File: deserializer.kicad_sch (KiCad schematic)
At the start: 0 parts

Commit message: [#51601] add deserializer
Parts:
- added C? (x5): C_10u_0402, antmicro-footprints:C_0402_1005Metric, symbol antmicroCapacitors0402:C_10u_0402
- added C? (x7): C_100n_0402, antmicro-footprints:C_0402_1005Metric, symbol antmicroCapacitors0402:C_100n_0402
- added C? (x5): C_10n_0402, antmicro-footprints:C_0402_1005Metric, symbol antmicroCapacitors0402:C_10n_0402
- added R? (x3): R_0R_0402, antmicro-footprints:R_0402_1005Metric, symbol antmicroResistors0402:R_0R_0402
- added R?: R_402R_0402, antmicro-footprints:R_0402_1005Metric, symbol antmicroResistors0402:R_402R_0402
- added U?: MAX96724GTN_VY+, antmicro-footprints:QFN-56-1EP_8x8mm_P0.5mm_EP4.8x4.8mm, symbol antmicroInterfaceControllers:MAX96724GTN_VY+
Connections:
- new net: C?.2, C?.2, C?.2, C?.2, C?.2, R?.1, U?.55 (VDD), U?.56 (VDD)
- new net: C?.2, C?.2, C?.2, C?.2, U?.20 (CAP_VDD), U?.8 (CAP_VDD)
- new net: C?.2, C?.2, C?.2, C?.2, C?.2, R?.1, U?.21 (VDD_1.8V), U?.7 (VDD_1.8V)
- new net: C?.2, C?.2, C?.2, R?.1, U?.24 (VDDIO)
- new net +1V8: R?.2
- new net GND: C?.1, C?.1, C?.1, C?.1, C?.1, C?.1, C?.1, C?.1, C?.1, C?.1, C?.1, C?.1, C?.1, C?.1, C?.1, C?.1, C?.1, U?.57 (GND)
- new net VDD: R?.2

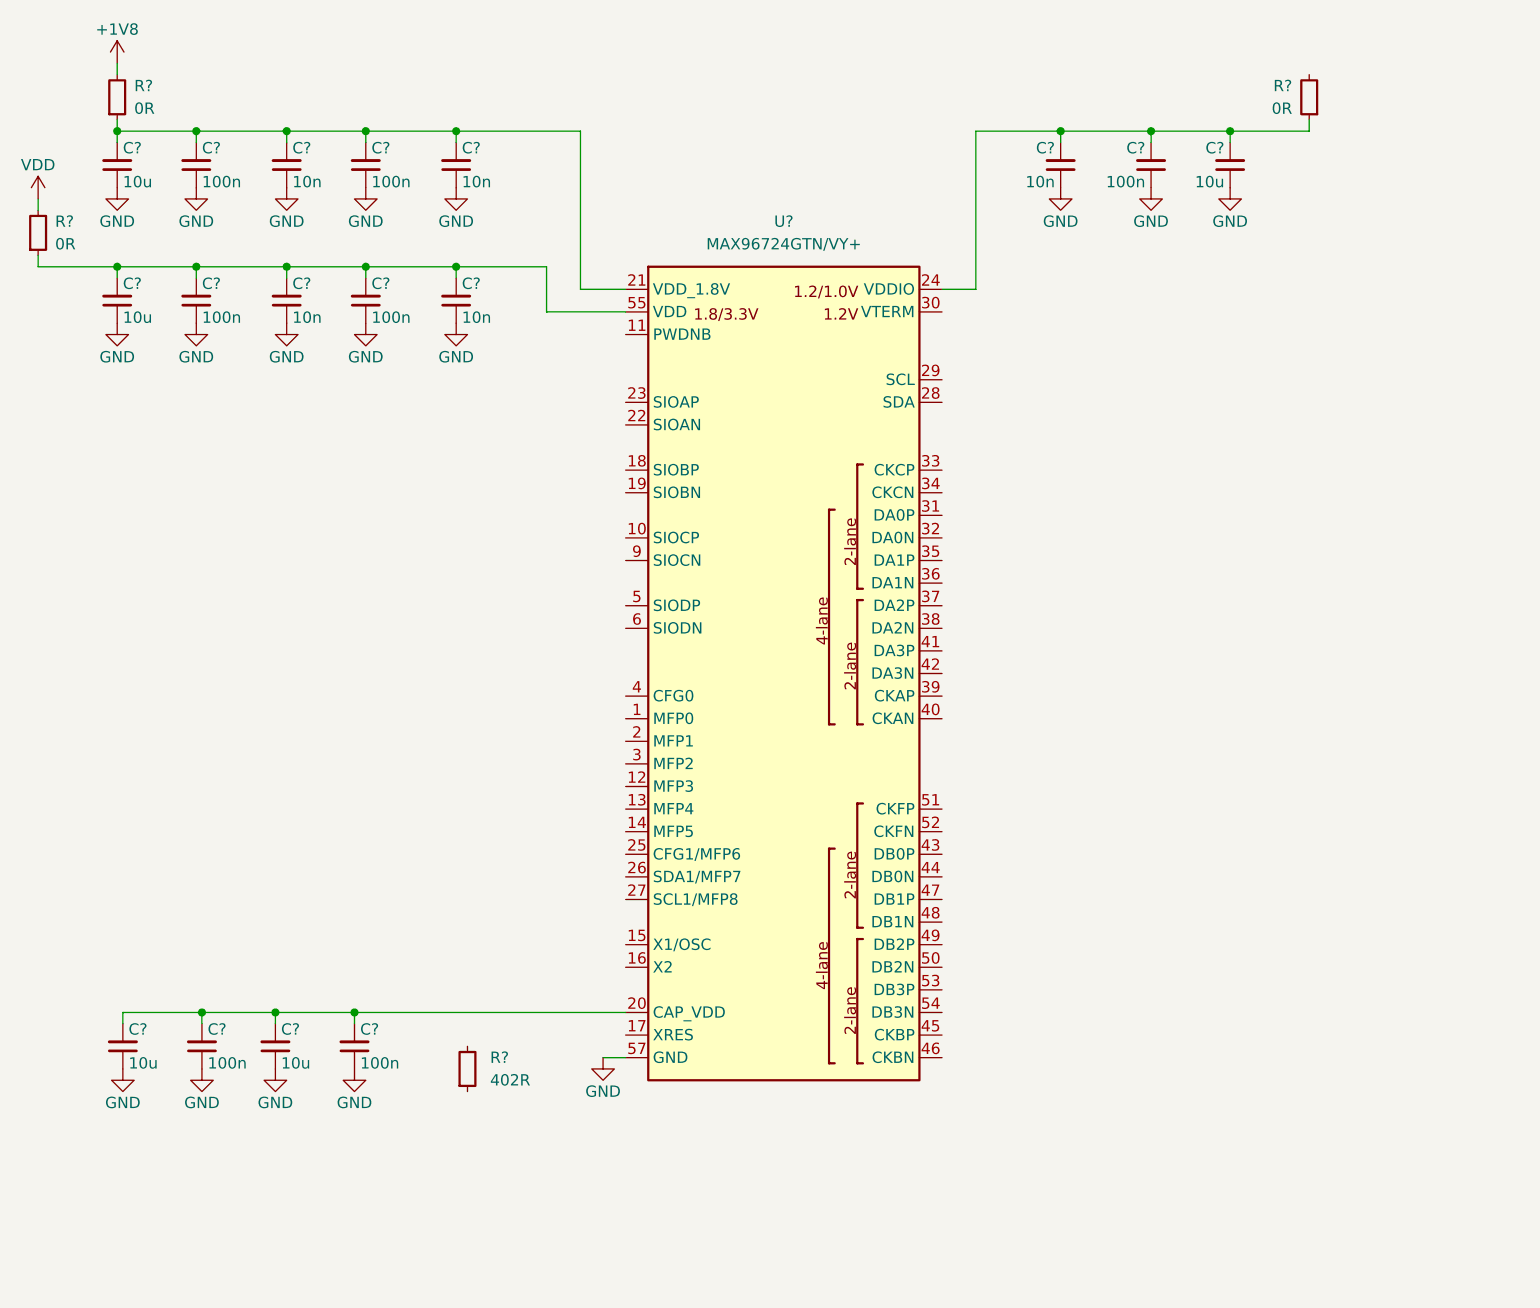
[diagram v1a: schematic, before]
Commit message: [#51627] Deserializer: add connections and passives
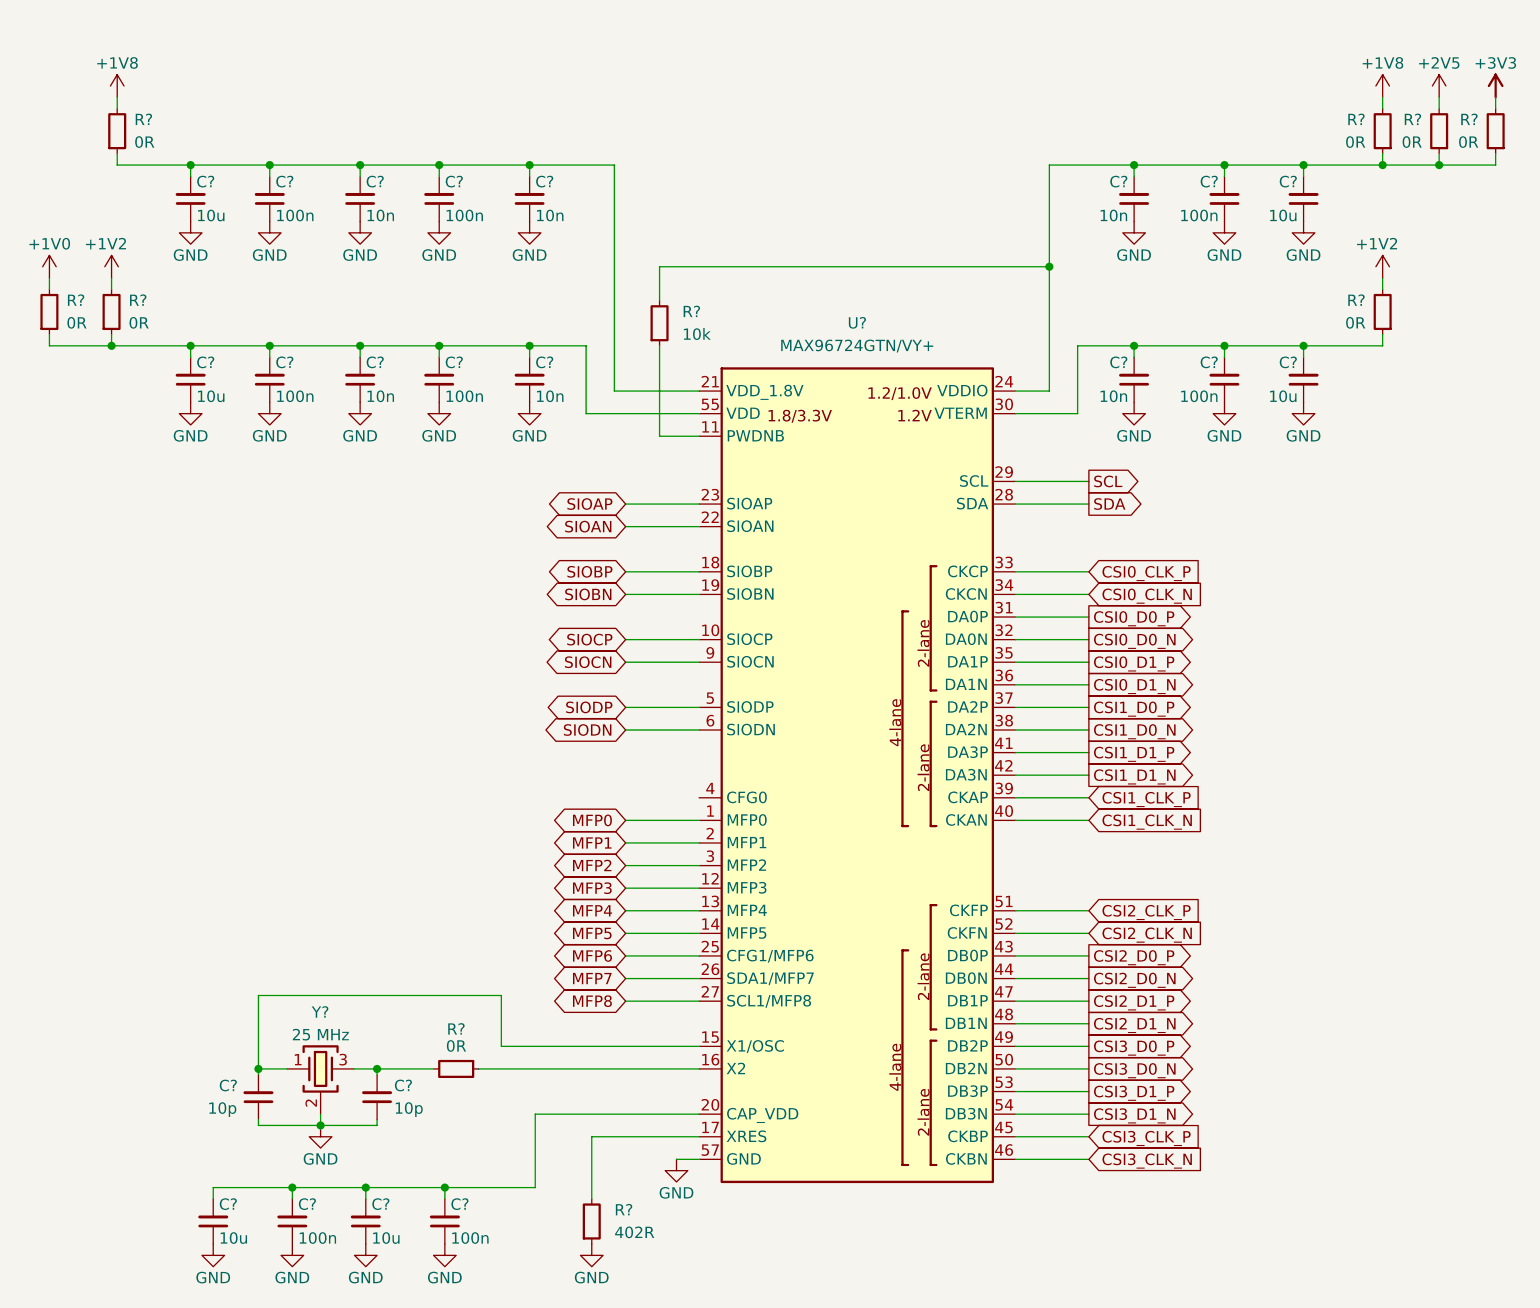
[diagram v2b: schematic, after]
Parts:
- added C? (x2): C_10p_0402, antmicro-footprints:C_0402_1005Metric, symbol antmicroCapacitors0402:C_10p_0402
- added C?: C_10u_0402, antmicro-footprints:C_0402_1005Metric, symbol antmicroCapacitors0402:C_10u_0402
- added C?: C_100n_0402, antmicro-footprints:C_0402_1005Metric, symbol antmicroCapacitors0402:C_100n_0402
- added C?: C_10n_0402, antmicro-footprints:C_0402_1005Metric, symbol antmicroCapacitors0402:C_10n_0402
- added R? (x5): R_0R_0402, antmicro-footprints:R_0402_1005Metric, symbol antmicroResistors0402:R_0R_0402
- added R?: R_10k_0402, antmicro-footprints:R_0402_1005Metric, symbol antmicroResistors0402:R_10k_0402
- added Y?: Resonator_25MHz_ABM8G, antmicro-footprints:Oscillator_SMD_Geyer_KX-7-4Pin_3.2x2.5mm, symbol antmicroResonators:Resonator_25MHz_ABM8G
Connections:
- net +1V8: now also R?.2
- net GND: now also R?.1, C?.1, C?.1, C?.1, C?.1, C?.1, Y?.2 (SH), Y?.4 (SH)
- net at C?.2, C?.2, C?.2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: now also R?.1
- net at C?.2, C?.2, C?.2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: now also R?.1, R?.1, R?.2
- net MFP0: now reaches U?.1 (MFP0)
- net SIOCP: now reaches U?.10 (SIOCP)
- net at U?.11 (PWDNB): now also R?.1
- net MFP3: now reaches U?.12 (MFP3)
- net MFP4: now reaches U?.13 (MFP4)
- net MFP5: now reaches U?.14 (MFP5)
- net at U?.15 (X1/OSC): now also C?.2, Y?.1
- net at U?.16 (X2): now also R?.1
- net at U?.17 (XRES): now also R?.2
- net SIOBP: now reaches U?.18 (SIOBP)
- net SIOBN: now reaches U?.19 (SIOBN)
- net MFP1: now reaches U?.2 (MFP1)
- net SIOAN: now reaches U?.22 (SIOAN)
- net SIOAP: now reaches U?.23 (SIOAP)
- net MFP6: now reaches U?.25 (CFG1/MFP6)
- net MFP7: now reaches U?.26 (SDA1/MFP7)
- net MFP8: now reaches U?.27 (SCL1/MFP8)
- net SDA: now reaches U?.28 (SDA)
- net SCL: now reaches U?.29 (SCL)
- net MFP2: now reaches U?.3 (MFP2)
- net at U?.30 (VTERM): now also C?.2, C?.2, C?.2, R?.1
- net CSI0_D0_P: now reaches U?.31 (DA0P)
- net CSI0_D0_N: now reaches U?.32 (DA0N)
- net CSI0_CLK_P: now reaches U?.33 (CKCP)
- net CSI0_CLK_N: now reaches U?.34 (CKCN)
- net CSI0_D1_P: now reaches U?.35 (DA1P)
- net CSI0_D1_N: now reaches U?.36 (DA1N)
- net CSI1_D0_P: now reaches U?.37 (DA2P)
- net CSI1_D0_N: now reaches U?.38 (DA2N)
- net CSI1_CLK_P: now reaches U?.39 (CKAP)
- net CSI1_CLK_N: now reaches U?.40 (CKAN)
- net CSI1_D1_P: now reaches U?.41 (DA3P)
- net CSI1_D1_N: now reaches U?.42 (DA3N)
- net CSI2_D0_P: now reaches U?.43 (DB0P)
- net CSI2_D0_N: now reaches U?.44 (DB0N)
- net CSI3_CLK_P: now reaches U?.45 (CKBP)
- net CSI3_CLK_N: now reaches U?.46 (CKBN)
- net CSI2_D1_P: now reaches U?.47 (DB1P)
- net CSI2_D1_N: now reaches U?.48 (DB1N)
- net CSI3_D0_P: now reaches U?.49 (DB2P)
- net SIODP: now reaches U?.5 (SIODP)
- net CSI3_D0_N: now reaches U?.50 (DB2N)
- net CSI2_CLK_P: now reaches U?.51 (CKFP)
- net CSI2_CLK_N: now reaches U?.52 (CKFN)
- net CSI3_D1_P: now reaches U?.53 (DB3P)
- net CSI3_D1_N: now reaches U?.54 (DB3N)
- net SIODN: now reaches U?.6 (SIODN)
- net SIOCN: now reaches U?.9 (SIOCN)
- net VDD renamed +1V2
- net +1V2: now also R?.2
- new net: C?.2, R?.2, Y?.3
- new net +1V0: R?.2
- new net +2V5: R?.2
- new net +3V3: R?.2
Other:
- company: (none) -> Antmicro Ltd
- title: (none) -> GMSL Deserializer
- moved on the sheet: C?, R?, U?

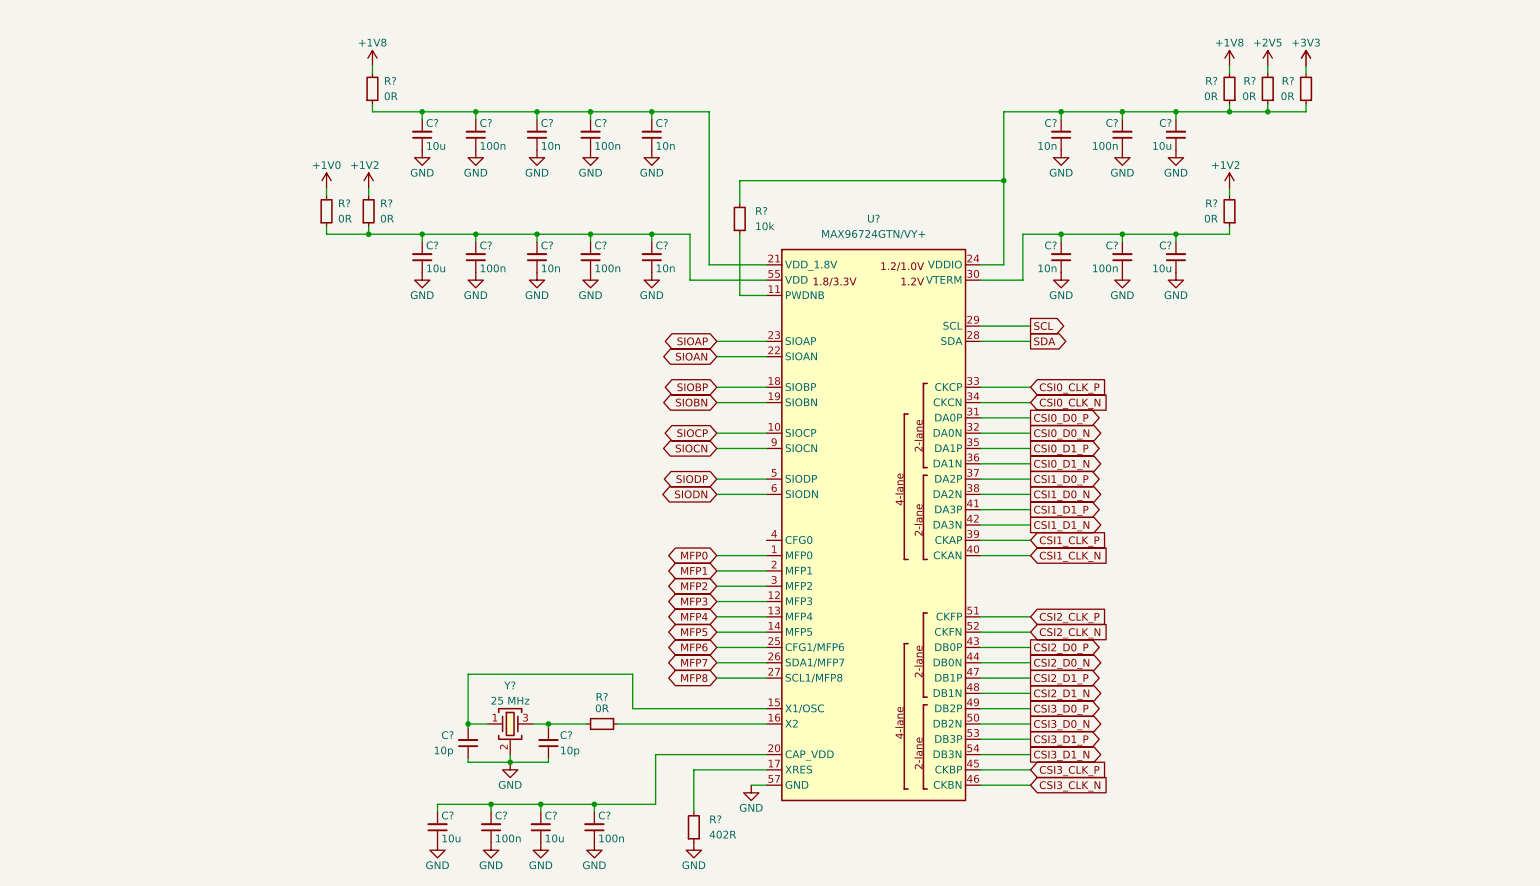
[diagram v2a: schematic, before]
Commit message: [#51627] Deserializer: change connections, add crystal and ESD diodes
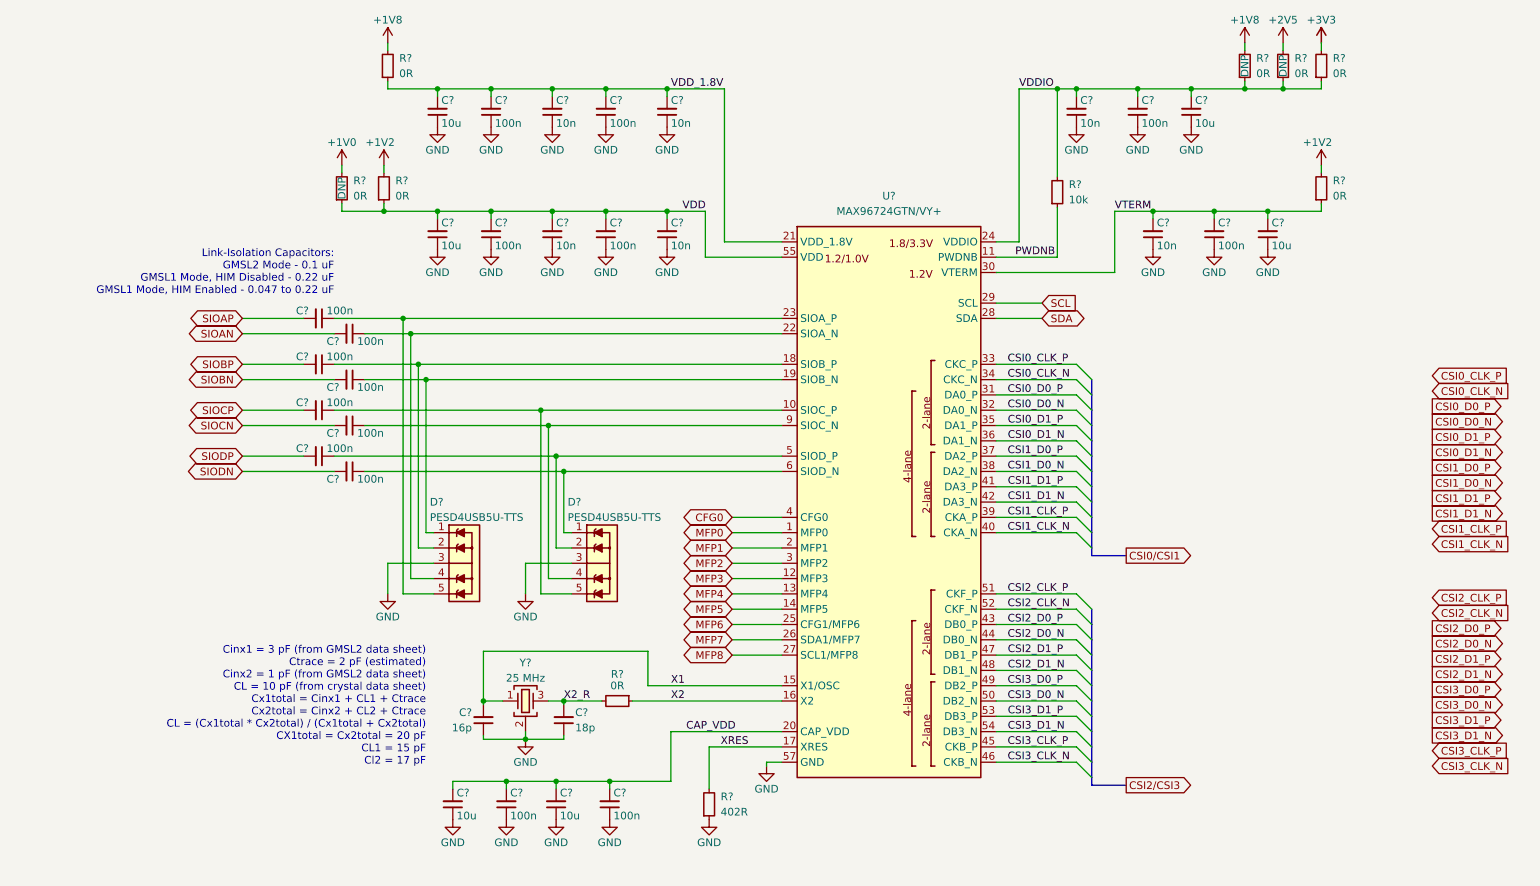
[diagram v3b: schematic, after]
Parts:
- removed C? (x2): C_10p_0402, antmicro-footprints:C_0402_1005Metric, symbol antmicroCapacitors0402:C_10p_0402
- removed R? (x2): R_0R_0402, antmicro-footprints:R_0402_1005Metric, symbol antmicroResistors0402:R_0R_0402
- added C? (x8): C_100n_0402, antmicro-footprints:C_0402_1005Metric, symbol antmicroCapacitors0402:C_100n_0402
- added C?: C_18p_0402, antmicro-footprints:C_0402_1005Metric, symbol antmicroCapacitors0402:C_18p_0402
- added C?: C_16p_0402, antmicro-footprints:C_0402_1005Metric, symbol antmicroCapacitors0402:C_16p_0402
- added D? (x2): PESD4USB5U-TTS, antmicro-footprints:DFN2510D-10, symbol antmicroTVSDiodes:PESD4USB5U-TTS
- added R? (x2): R_0R_0402, antmicro-footprints:R_0402_1005Metric, symbol antmicroResistors0402:R_0R_0402
- R?: DNP (none) -> DNP; now left out of the parts list
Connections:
- net +1V0: now also R?.2
- net +2V5: now also R?.2
- net GND: now also C?.1, C?.1, D?.3, D?.3, D?.8, D?.8
- net SIOAN: now also C?.2; no longer U?.22 (SIOAN)
- net SIOAP: now also C?.2; no longer U?.23 (SIOAP)
- net SIOBN: now also C?.2; no longer U?.19 (SIOBN)
- net SIOBP: now also C?.2; no longer U?.18 (SIOBP)
- net SIOCN: now also C?.2; no longer U?.9 (SIOCN)
- net SIOCP: now also C?.2; no longer U?.10 (SIOCP)
- net SIODN: now also C?.2; no longer U?.6 (SIODN)
- net SIODP: now also C?.2; no longer U?.5 (SIODP)
- net VDD: now reaches C?.2, C?.2, C?.2, C?.2, C?.2, R?.1, U?.55 (VDD), U?.56 (VDD)
- net VDD: now also R?.1
- net X2: now reaches R?.1, U?.16 (X2)
- net X2_R: now reaches R?.2, Y?.3
- net X2_R: now also C?.2
- net CAP_VDD: now reaches C?.2, C?.2, C?.2, C?.2, U?.20 (CAP_VDD), U?.8 (CAP_VDD)
- net VTERM: now reaches C?.2, C?.2, C?.2, R?.1, U?.30 (VTERM)
- net VDDIO: now reaches C?.2, C?.2, C?.2, R?.1, R?.1, R?.2, U?.24 (VDDIO)
- net VDDIO: now also R?.1
- net VDD_1.8V: now reaches C?.2, C?.2, C?.2, C?.2, C?.2, R?.1, U?.21 (VDD_1.8V), U?.7 (VDD_1.8V)
- net PWDNB: now reaches R?.1, U?.11 (PWDNB)
- net X1: now reaches U?.15 (X1/OSC), Y?.1
- net X1: now also C?.2
- net XRES: now reaches R?.2, U?.17 (XRES)
- net CFG0: now reaches U?.4 (CFG0)
- new net: C?.1, D?.5, U?.10 (SIOC_P)
- new net: C?.1, D?.2, U?.18 (SIOB_P)
- new net: C?.1, D?.1, U?.19 (SIOB_N)
- new net: C?.1, D?.4, U?.22 (SIOA_N)
- new net: C?.1, D?.5, U?.23 (SIOA_P)
- new net: C?.1, D?.1, U?.6 (SIOD_N)
- new net: C?.1, D?.2, U?.5 (SIOD_P)
- new net: C?.1, D?.4, U?.9 (SIOC_N)
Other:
- note added: "Cinx1 = 3 pF (from GMSL2 data sheet) Ctrace = 2 pF (estimated) Cinx2 = 1 pF (from GMSL2 data sheet) CL = 10 pF (from crystal data sheet) Cx1total = Cinx1 + CL1 + Ctrace Cx2total = Cinx2 + CL2 + Ctrace CL = (Cx1total * Cx2total) / (Cx1total + Cx2total) CX1total = Cx2total = 20 pF CL1 = 15 pF Cl2 = 17 pF"
- note added: "Link-Isolation Capacitors: GMSL2 Mode - 0.1 uF GMSL1 Mode, HIM Disabled - 0.22 uF GMSL1 Mode, HIM Enabled - 0.047 to 0.22 uF"
- moved on the sheet: C?, R?, U?, Y?
